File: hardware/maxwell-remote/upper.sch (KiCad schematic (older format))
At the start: 30 parts, among them J10 CAN, J11 SPI1_C, J12 SPI1_B, J13 Display, J14 SPI1_A, J15 Left, J16 Right, J3 ESPUART, J4 PROG, J6 ESPBOOT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

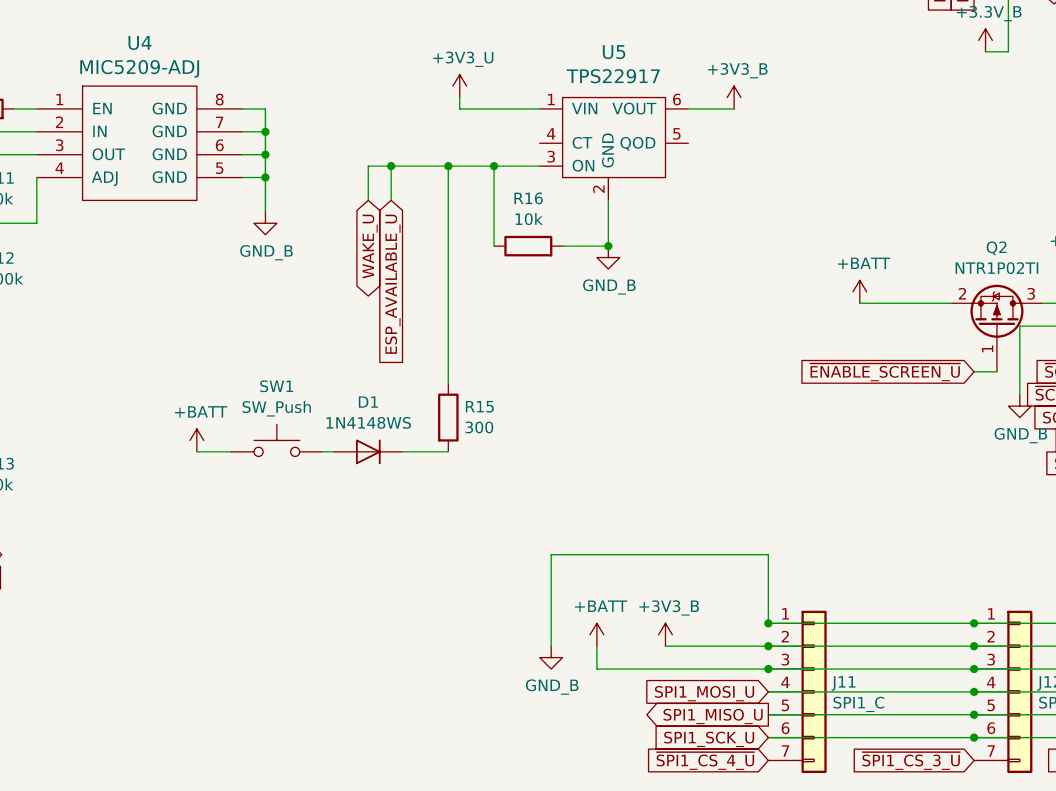
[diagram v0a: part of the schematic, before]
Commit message: Maxwell Remote v2.0.1
* Adds support for power-on by pressing handlebar button.
  The earlier design relied on the microcontroller waking
  when the button was pressed, but in this new switch
  configuration the microcontroller won't even be powered
  while the device is asleep, so we need to hard-wire
  the power button to the WAKE line.
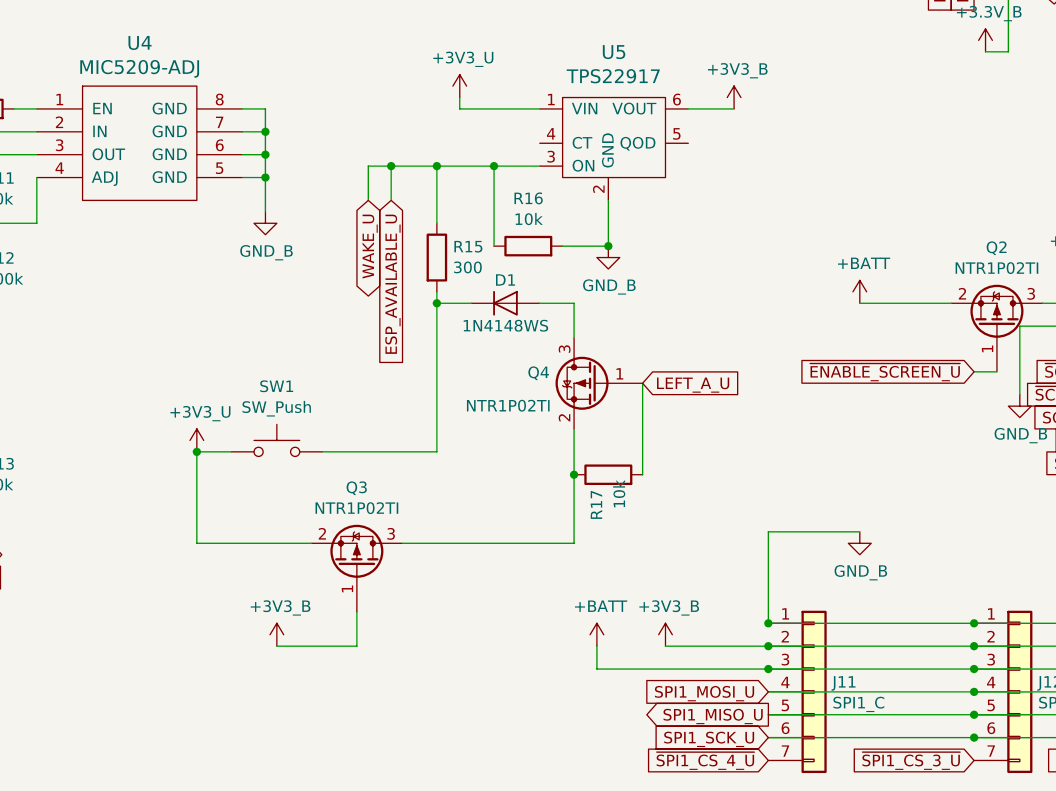
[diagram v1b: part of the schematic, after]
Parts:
- added Q3, Q4: NTR1P02TI, coddingtonbear:SOT-23_LargePads, symbol Device:Q_PMOS_GSD
- added R17: 10k, coddingtonbear:0805_Milling, symbol Device:R
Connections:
- net +3V3_B: now also Q3.1 (G)
- net +3V3_U: now also SW1.1, Q3.2 (S)
- net +BATT: no longer SW1.1
- net LEFT_A_U: now also Q4.1 (G), R17.2
- net at SW1.2: now also D1.1 (K), R15.2; no longer D1.2 (A)
- new net: Q3.3 (D), Q4.2 (S), R17.1
- new net: D1.2 (A), Q4.3 (D)
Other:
- moved on the sheet: R15
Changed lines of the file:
@@
 	5850 3350 5850 3000
 Connection ~ 5850 3000
-Wire Wire Line
-	5850 3000 5650 3000
 $Comp
 L coddingtonbear:+3V3_B #PWR0136
@@
 $EndComp
 $Comp
-L power:+BATT #PWR0137
-U 1 1 5C83DD9C
-P 4550 4250
-F 0 "#PWR0137" H 4550 4100 50  0001 C CNN
-F 1 "+BATT" H 4565 4423 50  0000 C CNN
-F 2 "" H 4550 4250 50  0001 C CNN
-F 3 "" H 4550 4250 50  0001 C CNN
-	1    4550 4250
-	1    0    0    -1
-$EndComp
-$Comp
-L Device:D D1
-U 1 1 5C83DEB2
-P 5300 4250
-F 0 "D1" H 5300 4034 50  0000 C CNN
-F 1 "1N4148WS" H 5300 4125 50  0000 C CNN
-F 2 "Diode_SMD:D_SOD-323_HandSoldering" H 5300 4250 50  0001 C CNN
-F 3 "~" H 5300 4250 50  0001 C CNN
-	1    5300 4250
-	-1   0    0    1
-$EndComp
-$Comp
 L Device:R R15
 U 1 1 5C83F469
-P 5650 4100
-F 0 "R15" H 5720 4146 50  0000 L CNN
-F 1 "300" H 5720 4055 50  0000 L CNN
-F 2 "coddingtonbear:0805_Milling" V 5580 4100 50  0001 C CNN
-F 3 "~" H 5650 4100 50  0001 C CNN
-	1    5650 4100
-	1    0    0    -1
-$EndComp
-Wire Wire Line
-	5650 3950 5650 3000
-Connection ~ 5650 3000
-Wire Wire Line
-	5650 3000 5400 3000
-Wire Wire Line
-	5650 4250 5450 4250
-Wire Wire Line
-	5150 4250 5100 4250
+P 5600 3400
+F 0 "R15" H 5670 3446 50  0000 L CNN
+F 1 "300" H 5670 3355 50  0000 L CNN
+F 2 "coddingtonbear:0805_Milling" V 5530 3400 50  0001 C CNN
+F 3 "~" H 5600 3400 50  0001 C CNN
+	1    5600 3400
+	1    0    0    -1
+$EndComp
 Wire Wire Line
 	4700 4250 4550 4250
@@
 L coddingtonbear:GND_B #PWR0148
 U 1 1 5C86C1EA
-P 6100 5100
-F 0 "#PWR0148" H 6100 4850 50  0001 C CNN
-F 1 "GND_B" H 6105 4927 50  0000 C CNN
-F 2 "" H 6100 5100 50  0001 C CNN
-F 3 "" H 6100 5100 50  0001 C CNN
-	1    6100 5100
-	1    0    0    -1
-$EndComp
-Wire Wire Line
-	7050 5000 7050 4700
-Wire Wire Line
-	7050 4700 6100 4700
-Wire Wire Line
-	6100 4700 6100 5100
+P 7450 4600
+F 0 "#PWR0148" H 7450 4350 50  0001 C CNN
+F 1 "GND_B" H 7455 4427 50  0000 C CNN
+F 2 "" H 7450 4600 50  0001 C CNN
+F 3 "" H 7450 4600 50  0001 C CNN
+	1    7450 4600
+	1    0    0    -1
+$EndComp
 Wire Wire Line
 	7050 5100 6600 5100
@@
 	7950 5000 7050 5000
 Connection ~ 7950 5000
-Connection ~ 7050 5000
 $Comp
 L coddingtonbear:+3V3_B #PWR0147
@@
 ESP_BOOT_MODE_U
 $Comp
-L coddingtonbear:GND_B #PWR?
+L coddingtonbear:GND_B #PWR0111
 U 1 1 5C8AD6CF
 P 10450 3800
-F 0 "#PWR?" H 10450 3550 50  0001 C CNN
+F 0 "#PWR0111" H 10450 3550 50  0001 C CNN
 F 1 "GND_B" H 10455 3627 50  0000 C CNN
 F 2 "" H 10450 3800 50  0001 C CNN
@@
 	1    0    0    -1
 $EndComp
+$Comp
+L coddingtonbear:+3V3_B #PWR0150
+U 1 1 5C8BDEA2
+P 4900 5100
+F 0 "#PWR0150" H 4900 4950 50  0001 C CNN
+F 1 "+3V3_B" H 4915 5273 50  0000 C CNN
+F 2 "" H 4900 5100 50  0001 C CNN
+F 3 "" H 4900 5100 50  0001 C CNN
+	1    4900 5100
+	1    0    0    -1
+$EndComp
+$Comp
+L Device:Q_PMOS_GSD Q3
+U 1 1 5C8DF4AD
+P 5250 4750
+F 0 "Q3" V 5593 4750 50  0000 C CNN
+F 1 "NTR1P02TI" V 5502 4750 50  0000 C CNN
+F 2 "coddingtonbear:SOT-23_LargePads" H 5450 4850 50  0001 C CNN
+F 3 "~" H 5250 4750 50  0001 C CNN
+	1    5250 4750
+	0    1    -1   0
+$EndComp
+$Comp
+L Device:R R17
+U 1 1 5C907638
+P 6350 4350
+F 0 "R17" H 6150 4400 50  0000 L CNN
+F 1 "10k" H 6200 4300 50  0000 L CNN
+F 2 "coddingtonbear:0805_Milling" V 6280 4350 50  0001 C CNN
+F 3 "~" H 6350 4350 50  0001 C CNN
+	1    6350 4350
+	0    -1   -1   0
+$EndComp
+Text GLabel 6500 3950 2    50   Input ~ 0
+LEFT_A_U
+$Comp
+L Device:Q_PMOS_GSD Q4
+U 1 1 5C96222A
+P 6300 3950
+F 0 "Q4" H 6506 3996 50  0000 L CNN
+F 1 "NTR1P02TI" H 6500 3850 50  0000 L CNN
+F 2 "coddingtonbear:SOT-23_LargePads" H 6500 4050 50  0001 C CNN
+F 3 "~" H 6300 3950 50  0001 C CNN
+	1    6300 3950
+	-1   0    0    -1
+$EndComp
+Wire Wire Line
+	6200 3750 6200 3600
+Wire Wire Line
+	5400 3000 5600 3000
+Wire Wire Line
+	5600 3250 5600 3000
+Connection ~ 5600 3000
+Wire Wire Line
+	5600 3000 5850 3000
+Wire Wire Line
+	7450 4600 7050 4600
+Wire Wire Line
+	7050 4600 7050 5000
+Connection ~ 7050 5000
+$Comp
+L coddingtonbear:+3V3_U #PWR0137
+U 1 1 5C9A2848
+P 4550 4250
+F 0 "#PWR0137" H 4550 4100 50  0001 C CNN
+F 1 "+3V3_U" H 4565 4423 50  0000 C CNN
+F 2 "" H 4550 4250 50  0001 C CNN
+F 3 "" H 4550 4250 50  0001 C CNN
+	1    4550 4250
+	1    0    0    -1
+$EndComp
+Connection ~ 4550 4250
+Wire Wire Line
+	5100 4250 5600 4250
+Wire Wire Line
+	6200 4150 6200 4350
+Wire Wire Line
+	4550 4250 4550 4650
+Wire Wire Line
+	5050 4650 4550 4650
+Wire Wire Line
+	5250 4950 5250 5100
+Wire Wire Line
+	5250 5100 4900 5100
+Wire Wire Line
+	6500 4350 6500 3950
+Wire Wire Line
+	6200 4350 6200 4650
+Wire Wire Line
+	6200 4650 5450 4650
+Connection ~ 6200 4350
+Wire Wire Line
+	5600 3550 5600 3600
+$Comp
+L Device:D D1
+U 1 1 5C9F3582
+P 5900 3600
+F 0 "D1" H 5900 3700 50  0000 C CNN
+F 1 "1N4148WS" H 5900 3500 50  0000 C CNN
+F 2 "Diode_SMD:D_SOD-323_HandSoldering" H 5900 3600 50  0001 C CNN
+F 3 "~" H 5900 3600 50  0001 C CNN
+	1    5900 3600
+	1    0    0    -1
+$EndComp
+Wire Wire Line
+	6200 3600 6050 3600
+Wire Wire Line
+	5750 3600 5600 3600
+Connection ~ 5600 3600
+Wire Wire Line
+	5600 3600 5600 4250
 $EndSCHEMATC

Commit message: Maxwell Remote v2.0.2
* Switches off power to SPI-connected devices when powered-down.
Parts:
- added Q5: NTR1P02TI, coddingtonbear:SOT-23_LargePads, symbol Device:Q_PMOS_GSD
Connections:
- net ESP_AVAILABLE_U: now also Q5.1 (G)
- net GND_B: now also Q5.3 (D); no longer J11.1 (Pin_1), J12.1 (Pin_1), J13.2 (Pin_2), J14.1 (Pin_1)
- new net: J11.1 (Pin_1), J12.1 (Pin_1), J13.2 (Pin_2), J14.1 (Pin_1), Q5.2 (S)
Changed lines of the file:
@@
 	8800 3600 8250 3600
-$Comp
-L coddingtonbear:GND_B #PWR0145
-U 1 1 5C863C4D
-P 8150 4000
-F 0 "#PWR0145" H 8150 3750 50  0001 C CNN
-F 1 "GND_B" H 8155 3827 50  0000 C CNN
-F 2 "" H 8150 4000 50  0001 C CNN
-F 3 "" H 8150 4000 50  0001 C CNN
-	1    8150 4000
-	1    0    0    -1
-$EndComp
 $Comp
 L coddingtonbear:+3V3_B #PWR0146
@@
 Text GLabel 8800 3900 0    50   Input ~ 0
 ~SCREEN_CS_U
-Wire Wire Line
-	8150 3700 8150 4000
 Wire Wire Line
 	8150 3700 8800 3700
@@
 L coddingtonbear:GND_B #PWR0148
 U 1 1 5C86C1EA
-P 7450 4600
-F 0 "#PWR0148" H 7450 4350 50  0001 C CNN
-F 1 "GND_B" H 7455 4427 50  0000 C CNN
-F 2 "" H 7450 4600 50  0001 C CNN
-F 3 "" H 7450 4600 50  0001 C CNN
-	1    7450 4600
+P 8250 4600
+F 0 "#PWR0148" H 8250 4350 50  0001 C CNN
+F 1 "GND_B" H 8255 4427 50  0000 C CNN
+F 2 "" H 8250 4600 50  0001 C CNN
+F 3 "" H 8250 4600 50  0001 C CNN
+	1    8250 4600
 	1    0    0    -1
 $EndComp
@@
 Wire Wire Line
 	5600 3600 5600 4250
+$Comp
+L Device:Q_PMOS_GSD Q5
+U 1 1 5C9FCE95
+P 7650 4500
+F 0 "Q5" V 7900 4500 50  0000 C CNN
+F 1 "NTR1P02TI" V 7991 4500 50  0000 C CNN
+F 2 "coddingtonbear:SOT-23_LargePads" H 7850 4600 50  0001 C CNN
+F 3 "~" H 7650 4500 50  0001 C CNN
+	1    7650 4500
+	0    1    1    0
+$EndComp
+Wire Wire Line
+	7850 4600 8250 4600
+Text GLabel 7650 4300 0    50   BiDi ~ 0
+WAKE_U
+Wire Wire Line
+	8150 3700 8150 4200
+Wire Wire Line
+	8150 4200 7050 4200
+Wire Wire Line
+	7050 4200 7050 4600
+Connection ~ 7050 4600
 $EndSCHEMATC

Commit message: Maxwell Remote v2.0.3
* Fixes schematic such that an N-Channel mosfet is used for
  controlling the GND side of the SPI expansion ports.
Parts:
- removed Q5: NTR1P02TI, coddingtonbear:SOT-23_LargePads, symbol Device:Q_PMOS_GSD
- added Q5: BSS138P, coddingtonbear:SOT-23_LargePads, symbol Device:Q_NMOS_GSD
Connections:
- net ESP_AVAILABLE_U: now also Q5.1 (G)
- net GND_B: now also Q5.2 (S)
- net at J11.1 (Pin_1), J12.1 (Pin_1), J13.2 (Pin_2)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: now also Q5.3 (D)
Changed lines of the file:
@@
 Wire Wire Line
 	5600 3600 5600 4250
-$Comp
-L Device:Q_PMOS_GSD Q5
-U 1 1 5C9FCE95
-P 7650 4500
-F 0 "Q5" V 7900 4500 50  0000 C CNN
-F 1 "NTR1P02TI" V 7991 4500 50  0000 C CNN
-F 2 "coddingtonbear:SOT-23_LargePads" H 7850 4600 50  0001 C CNN
-F 3 "~" H 7650 4500 50  0001 C CNN
-	1    7650 4500
-	0    1    1    0
-$EndComp
 Wire Wire Line
 	7850 4600 8250 4600
@@
 	7050 4200 7050 4600
 Connection ~ 7050 4600
+$Comp
+L Device:Q_NMOS_GSD Q5
+U 1 1 5CA10F3A
+P 7650 4500
+F 0 "Q5" V 7900 4500 50  0000 C CNN
+F 1 "BSS138P" V 7991 4500 50  0000 C CNN
+F 2 "coddingtonbear:SOT-23_LargePads" H 7850 4600 50  0001 C CNN
+F 3 "~" H 7650 4500 50  0001 C CNN
+	1    7650 4500
+	0    -1   1    0
+$EndComp
 $EndSCHEMATC

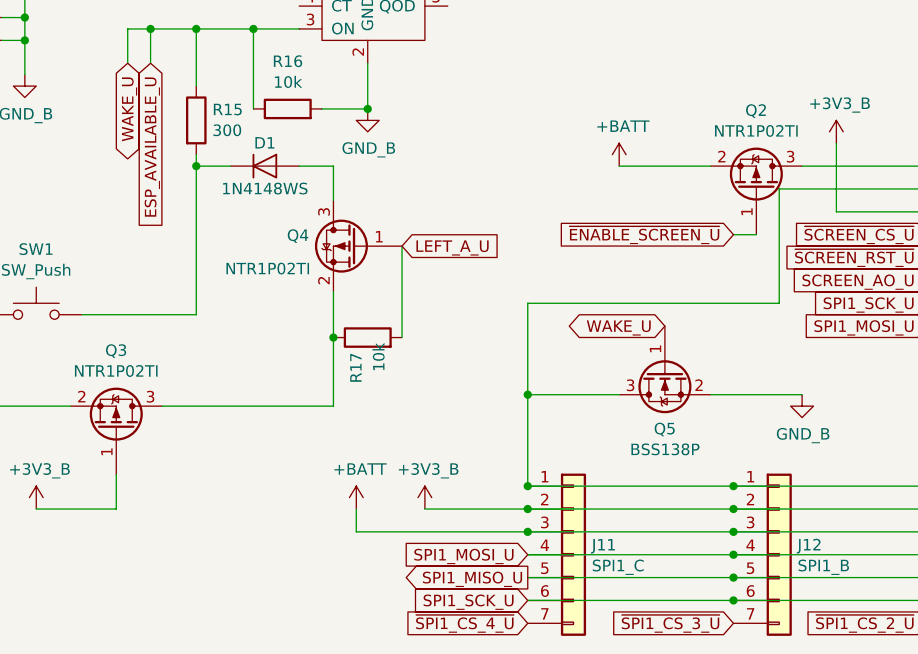
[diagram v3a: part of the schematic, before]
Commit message: Fixing errata:
* Adding 10k pulldown for ENABLE_DISPLAY (backlight control).
* Adding 2u capacitor to PDOWN_PU to ensure WAKE is pulled high
  for long enough for the microcontroller to start.
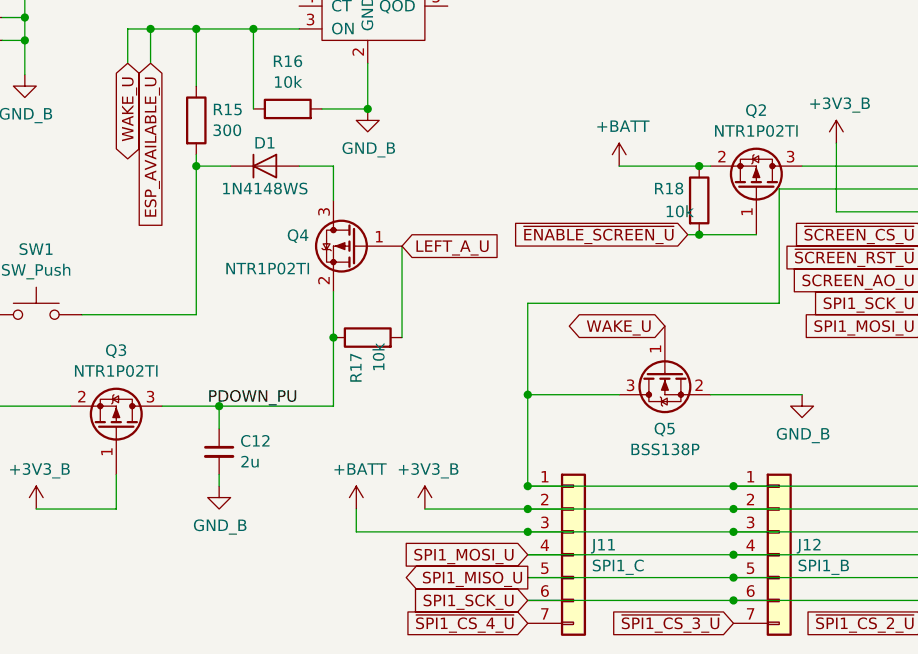
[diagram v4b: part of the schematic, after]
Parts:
- added C12: 2u, coddingtonbear:0805_Milling, symbol Device:C_Small
- added R18: 10k, coddingtonbear:0805_Milling, symbol Device:R
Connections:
- net +BATT: now also R18.1
- net GND_B: now also C12.2
- net ~ENABLE_SCREEN_U: now also R18.2
- net PDOWN_PU: now reaches Q3.3 (D), Q4.2 (S), R17.1
- net PDOWN_PU: now also C12.1
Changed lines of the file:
@@
 EESchema Schematic File Version 4
 LIBS:maxwell-remote-cache
-LIBS:maxwell-remote-2-cache
 EELAYER 26 0
 EELAYER END
@@
 	0    1    -1   0
 $EndComp
-Text GLabel 7950 3900 0    50   Input ~ 0
+Text GLabel 7750 3900 0    50   Input ~ 0
 ~ENABLE_SCREEN_U
-Wire Wire Line
-	8050 3900 7950 3900
 $Comp
 L power:+BATT #PWR0144
@@
 $EndComp
 Wire Wire Line
-	7850 3600 7450 3600
+	7850 3600 7800 3600
 Wire Wire Line
 	8800 3600 8250 3600
@@
 	6200 4350 6200 4650
 Wire Wire Line
-	6200 4650 5450 4650
+	6200 4650 5700 4650
 Connection ~ 6200 4350
 Wire Wire Line
@@
 	0    -1   1    0
 $EndComp
+Text Label 5650 4650 0    50   ~ 0
+PDOWN_PU
+$Comp
+L Device:C_Small C12
+U 1 1 5CA289C7
+P 5700 4850
+F 0 "C12" H 5792 4896 50  0000 L CNN
+F 1 "2u" H 5792 4805 50  0000 L CNN
+F 2 "coddingtonbear:0805_Milling" H 5700 4850 50  0001 C CNN
+F 3 "~" H 5700 4850 50  0001 C CNN
+	1    5700 4850
+	1    0    0    -1
+$EndComp
+$Comp
+L coddingtonbear:GND_B #PWR0145
+U 1 1 5CA28A63
+P 5700 5000
+F 0 "#PWR0145" H 5700 4750 50  0001 C CNN
+F 1 "GND_B" H 5705 4827 50  0000 C CNN
+F 2 "" H 5700 5000 50  0001 C CNN
+F 3 "" H 5700 5000 50  0001 C CNN
+	1    5700 5000
+	1    0    0    -1
+$EndComp
+Wire Wire Line
+	5700 5000 5700 4950
+Wire Wire Line
+	5700 4750 5700 4650
+Connection ~ 5700 4650
+Wire Wire Line
+	5700 4650 5450 4650
+$Comp
+L Device:R R18
+U 1 1 5CA31DAF
+P 7800 3750
+F 0 "R18" H 7600 3800 50  0000 L CNN
+F 1 "10k" H 7650 3700 50  0000 L CNN
+F 2 "coddingtonbear:0805_Milling" V 7730 3750 50  0001 C CNN
+F 3 "~" H 7800 3750 50  0001 C CNN
+	1    7800 3750
+	1    0    0    -1
+$EndComp
+Connection ~ 7800 3600
+Wire Wire Line
+	7800 3600 7450 3600
+Wire Wire Line
+	7800 3900 8050 3900
+Wire Wire Line
+	7750 3900 7800 3900
+Connection ~ 7800 3900
 $EndSCHEMATC

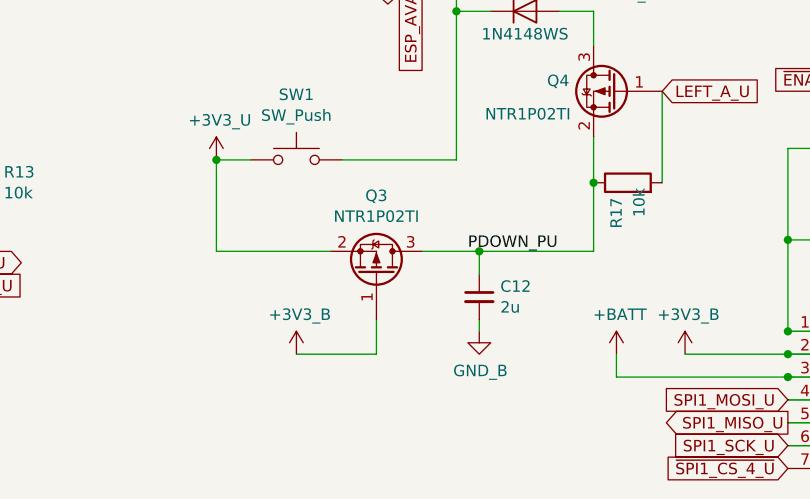
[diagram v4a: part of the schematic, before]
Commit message: Fix: Removes weird pull-up-only-on-power-down for LEFT_A; instead just always pulls up LEFT_A.
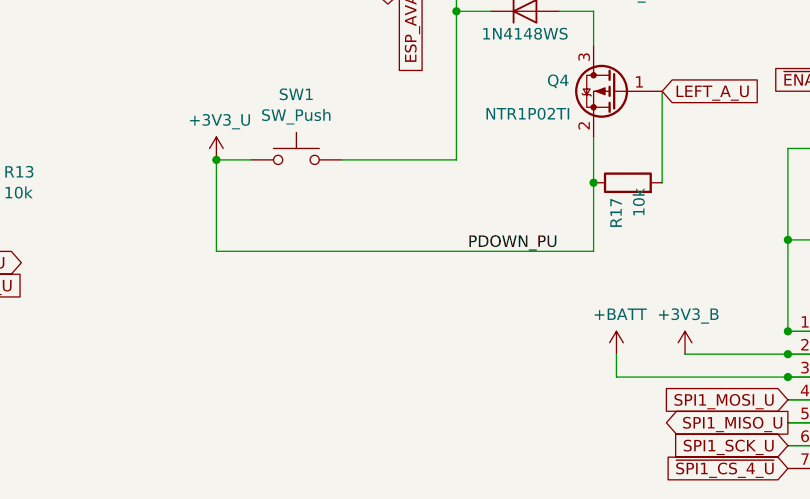
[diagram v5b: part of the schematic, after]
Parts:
- removed C12: 2u, coddingtonbear:0805_Milling, symbol Device:C_Small
- removed Q3: NTR1P02TI, coddingtonbear:SOT-23_LargePads, symbol Device:Q_PMOS_GSD
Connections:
- net PDOWN_PU is gone; now on net +3V3_U: Q4.2 (S), R17.1
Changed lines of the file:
@@
-$EndComp
-$Comp
-L coddingtonbear:+3V3_B #PWR0150
-U 1 1 5C8BDEA2
-P 4900 5100
-F 0 "#PWR0150" H 4900 4950 50  0001 C CNN
-F 1 "+3V3_B" H 4915 5273 50  0000 C CNN
-F 2 "" H 4900 5100 50  0001 C CNN
-F 3 "" H 4900 5100 50  0001 C CNN
-	1    4900 5100
-	1    0    0    -1
-$EndComp
-$Comp
-L Device:Q_PMOS_GSD Q3
-U 1 1 5C8DF4AD
-P 5250 4750
-F 0 "Q3" V 5593 4750 50  0000 C CNN
-F 1 "NTR1P02TI" V 5502 4750 50  0000 C CNN
-F 2 "coddingtonbear:SOT-23_LargePads" H 5450 4850 50  0001 C CNN
-F 3 "~" H 5250 4750 50  0001 C CNN
-	1    5250 4750
-	0    1    -1   0
 $EndComp
 $Comp
@@
 	4550 4250 4550 4650
 Wire Wire Line
-	5050 4650 4550 4650
-Wire Wire Line
-	5250 4950 5250 5100
-Wire Wire Line
-	5250 5100 4900 5100
-Wire Wire Line
 	6500 4350 6500 3950
 Wire Wire Line
 	6200 4350 6200 4650
-Wire Wire Line
-	6200 4650 5700 4650
 Connection ~ 6200 4350
 Wire Wire Line
@@
 PDOWN_PU
 $Comp
-L Device:C_Small C12
-U 1 1 5CA289C7
-P 5700 4850
-F 0 "C12" H 5792 4896 50  0000 L CNN
-F 1 "2u" H 5792 4805 50  0000 L CNN
-F 2 "coddingtonbear:0805_Milling" H 5700 4850 50  0001 C CNN
-F 3 "~" H 5700 4850 50  0001 C CNN
-	1    5700 4850
-	1    0    0    -1
-$EndComp
-$Comp
-L coddingtonbear:GND_B #PWR0145
-U 1 1 5CA28A63
-P 5700 5000
-F 0 "#PWR0145" H 5700 4750 50  0001 C CNN
-F 1 "GND_B" H 5705 4827 50  0000 C CNN
-F 2 "" H 5700 5000 50  0001 C CNN
-F 3 "" H 5700 5000 50  0001 C CNN
-	1    5700 5000
-	1    0    0    -1
-$EndComp
-Wire Wire Line
-	5700 5000 5700 4950
-Wire Wire Line
-	5700 4750 5700 4650
-Connection ~ 5700 4650
-Wire Wire Line
-	5700 4650 5450 4650
-$Comp
 L Device:R R18
 U 1 1 5CA31DAF
@@
 	7750 3900 7800 3900
 Connection ~ 7800 3900
+Wire Wire Line
+	4550 4650 6200 4650
 $EndSCHEMATC
